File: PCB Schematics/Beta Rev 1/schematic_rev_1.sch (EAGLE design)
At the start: 10 parts, among them IC1 STM8S003F3

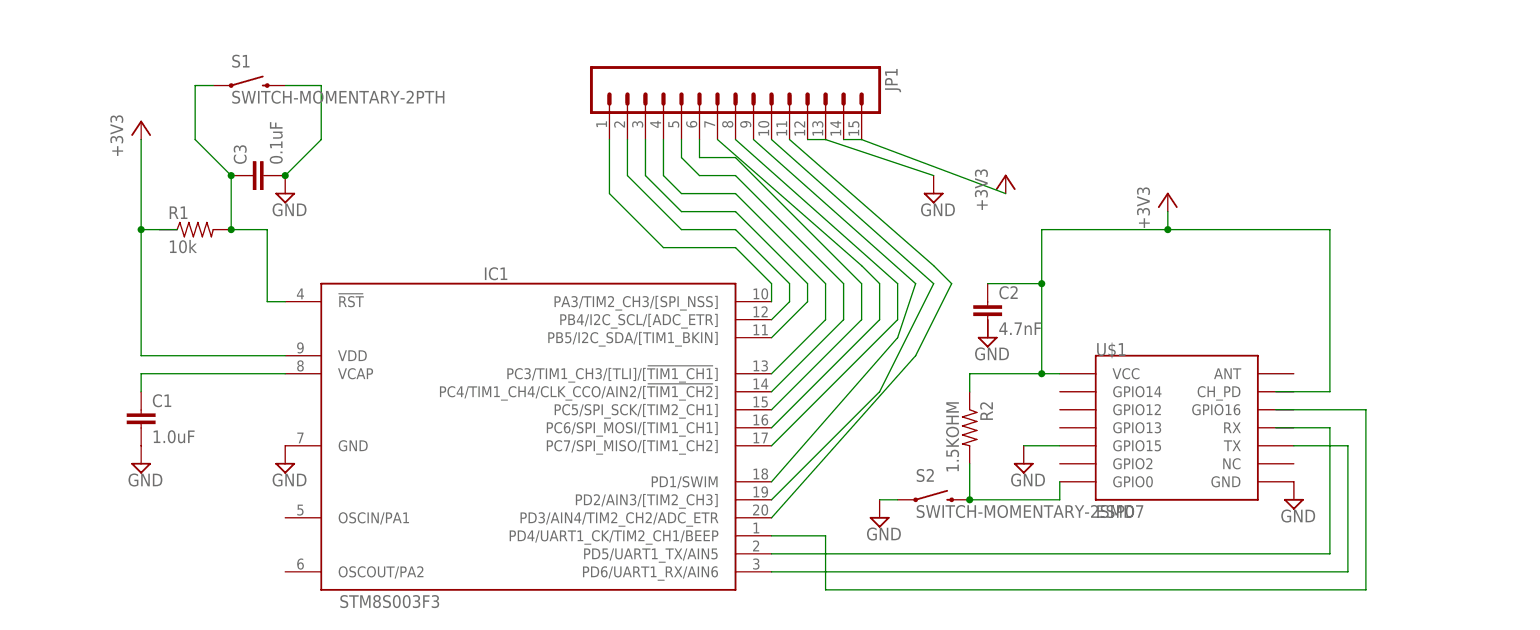
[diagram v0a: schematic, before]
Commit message: Updated schematic by Manivannan. Corrected component placements and cleaned up the nets.
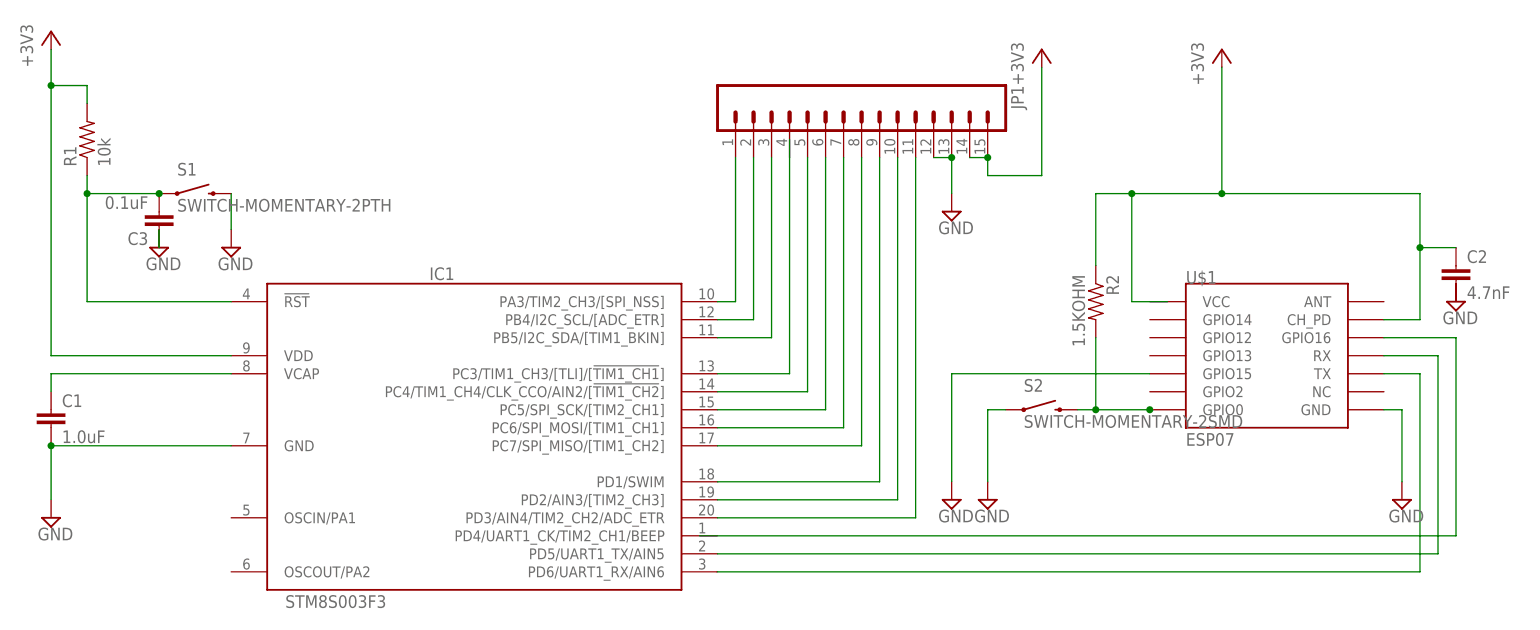
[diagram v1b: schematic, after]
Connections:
- removed net N$2: IC1.PD5/UART1_TX/AIN5
- removed net N$7 (its old number): IC1.PD4/UART1_CK/TIM2_CH1/BEEP
- new net N$18: C3.2, IC1.!RST, R1.1, S1.1
- new net N$5: IC1.PD5/UART1_TX/AIN5, U$1.RX
- net +3V3: now also R1.2, U$1.CH_PD; no longer U$1.VCC
- net GND: now also C3.1; no longer C3.2
- net N$4: now also U$1.GPIO16; no longer C3.1, IC1.!RST, R1.2, S1.1
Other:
- moved on the sheet: C1, C2, C3, IC1, JP1, R1, R2, S1, S2, U$1
